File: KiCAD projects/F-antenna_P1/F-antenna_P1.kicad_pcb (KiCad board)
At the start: 2 copper layers, 4.5 x 3.5 mm, 1 part, among them J1 MMCX_Connector

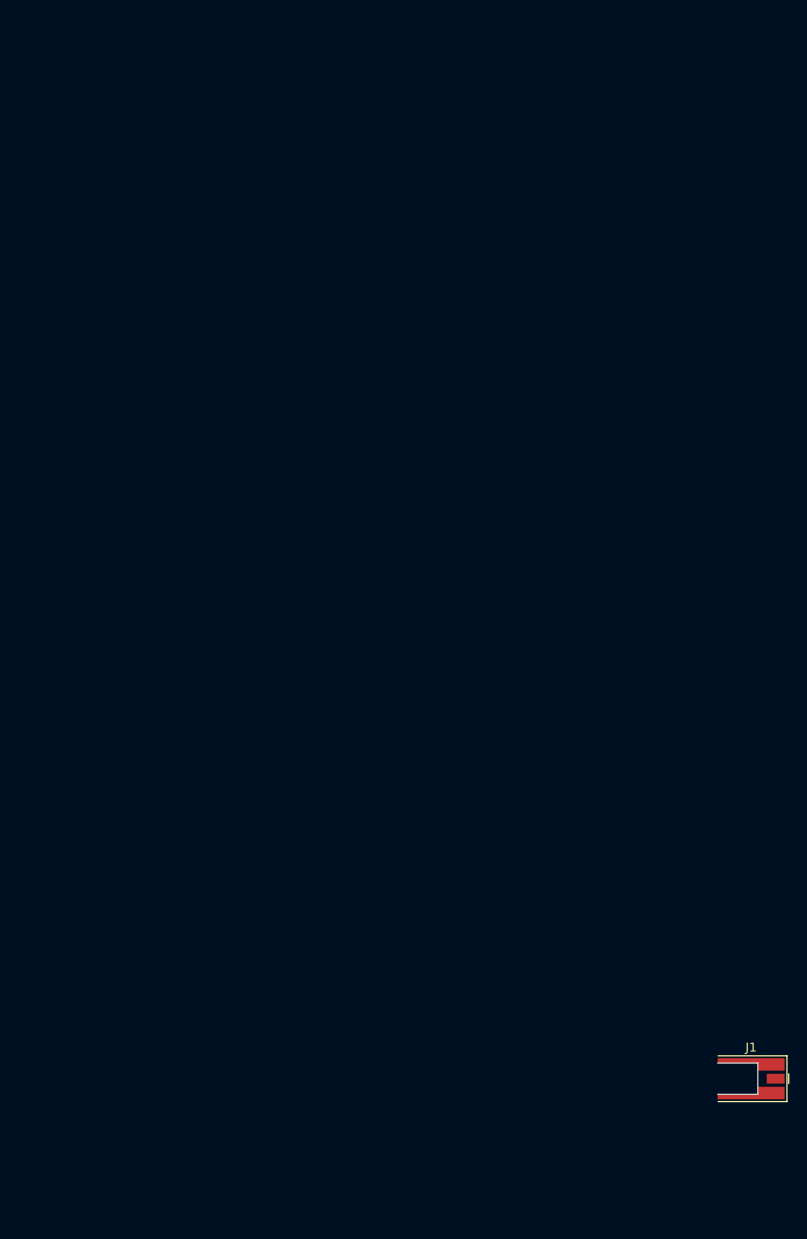
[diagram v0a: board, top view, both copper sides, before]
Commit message: Created PCB PIFA prototype 1
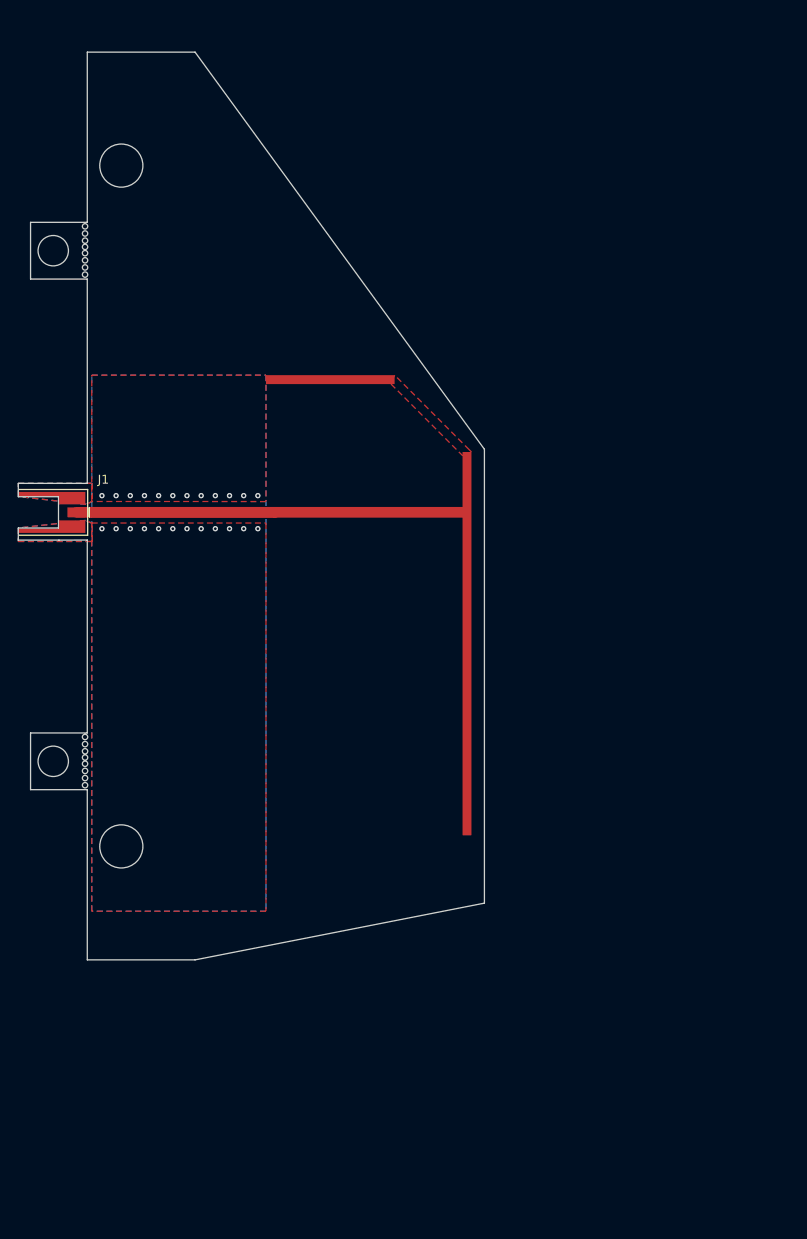
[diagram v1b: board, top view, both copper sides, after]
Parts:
- moved J1 100.7 mm to (65.9, 89.6)
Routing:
- net GroundPlane: track 0.00 -> 22.2 mm, vias 0 -> 24
- added copper zone on B.Cu, net GroundPlane
- added copper zone on F.Cu, net GroundPlane
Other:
- board size 4.5 x 3.5 mm -> 52.2 x 101.6 mm

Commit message: Updated PCB files to match new mold
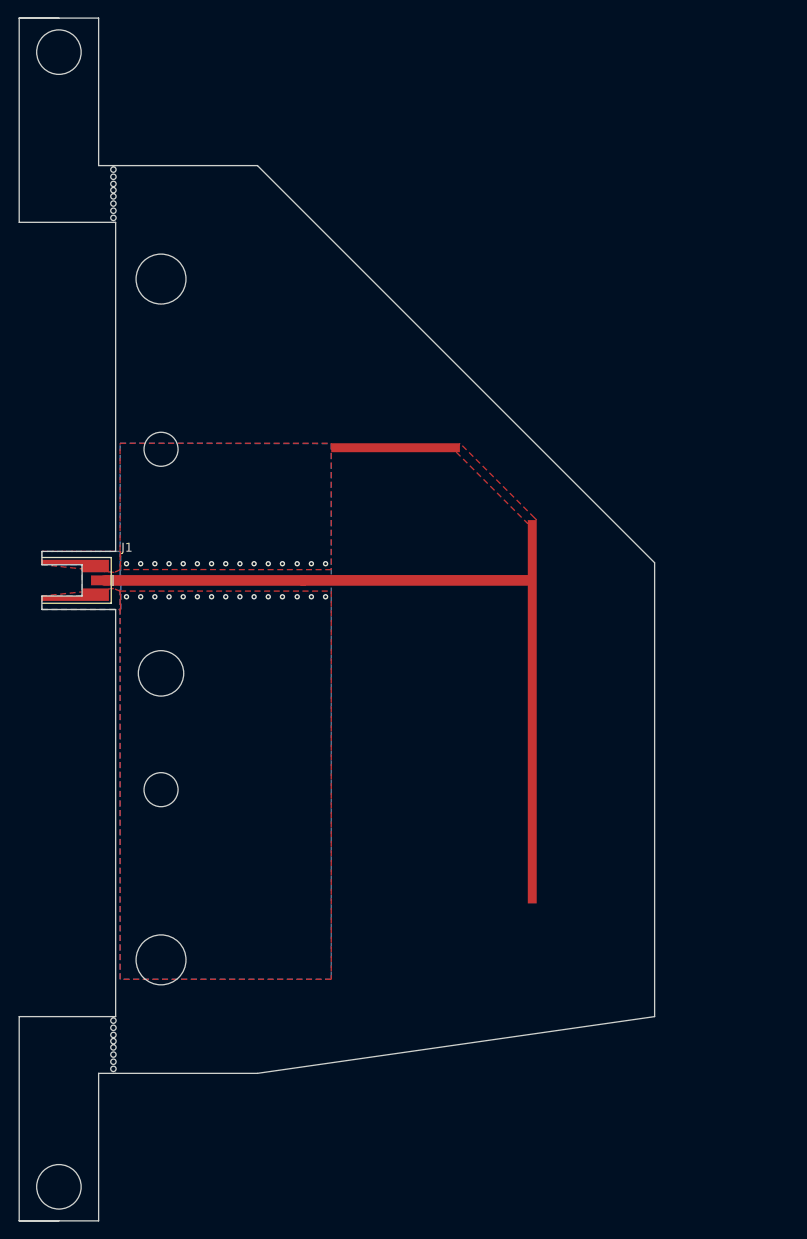
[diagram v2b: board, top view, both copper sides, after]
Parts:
- moved J1 8.06 mm to (68.5, 97.2)
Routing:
- net GroundPlane: track 22.2 -> 47.5 mm, vias 24 -> 30
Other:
- board size 52.2 x 101.6 mm -> 71.1 x 134.6 mm
